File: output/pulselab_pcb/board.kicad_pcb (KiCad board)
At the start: 2 copper layers, 60 x 60 mm, 17 parts

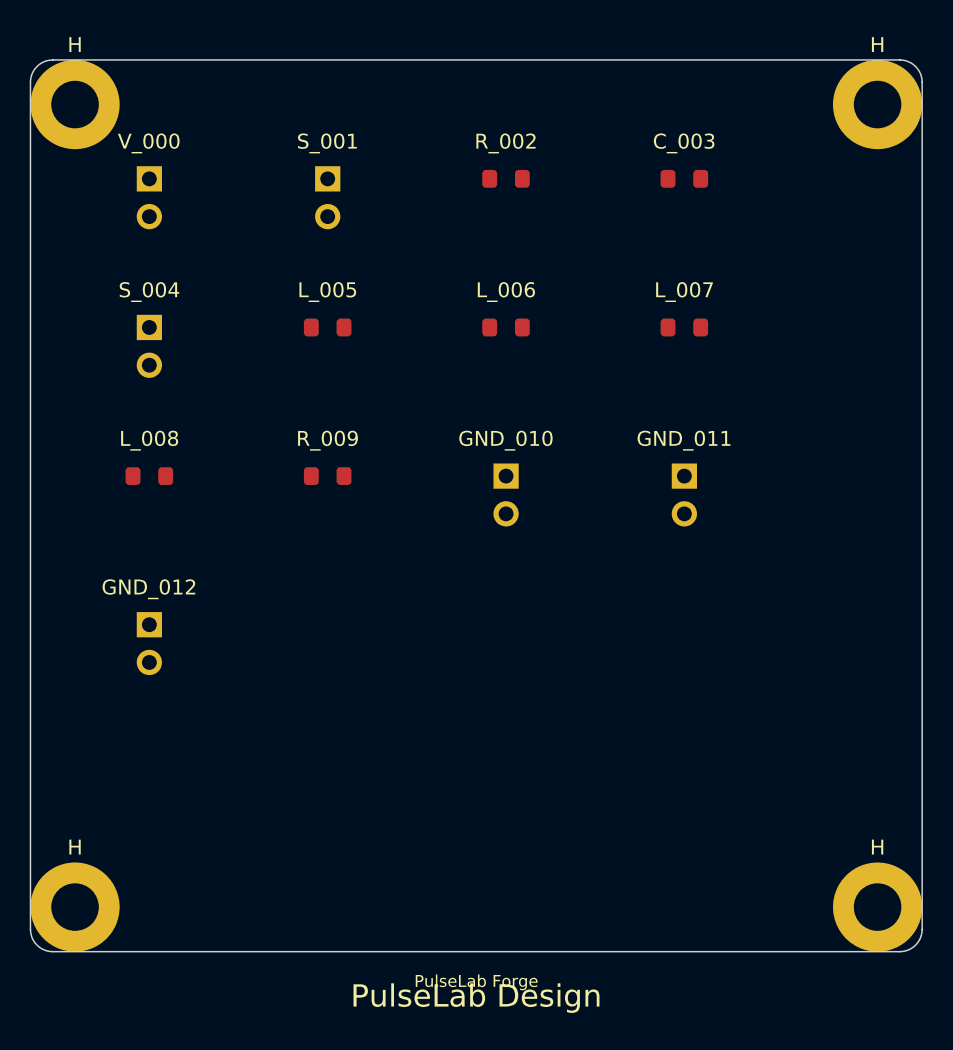
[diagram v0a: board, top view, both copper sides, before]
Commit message: chore: update dependencies and project artifacts
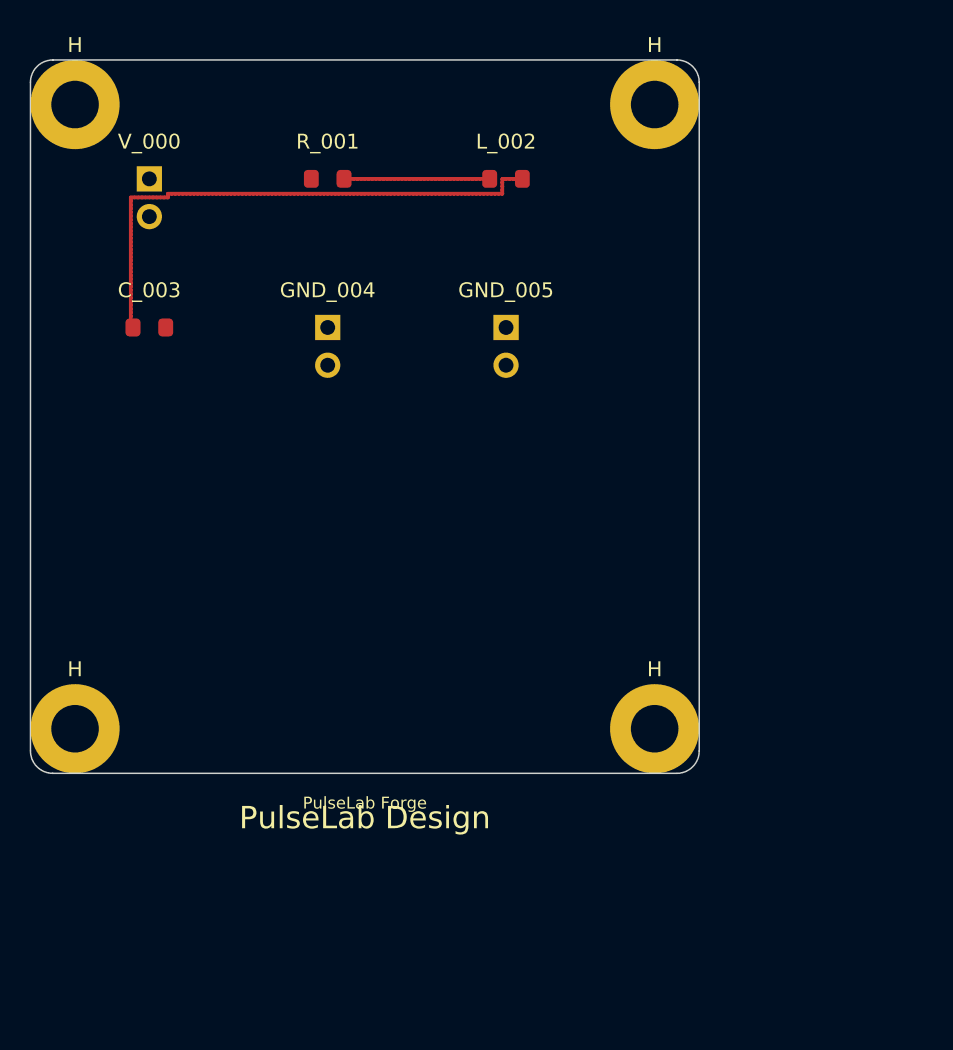
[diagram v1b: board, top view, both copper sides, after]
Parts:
- removed GND_010, GND_011, GND_012: GND, Connector_PinHeader_2.54mm:PinHeader_1x02_P2.54mm_Vertical
- removed the H at (57.0, 3.00)
- removed the H at (3.00, 57.0)
- removed the H at (57.0, 57.0)
- removed L_005, L_006, L_007, L_008: 2.5e-07, Inductor_SMD:L_0805_2012Metric
- removed R_002: 10000, Resistor_SMD:R_0805_2012Metric
- removed R_009: 50, Resistor_SMD:R_0805_2012Metric
- removed S_001, S_004: S, Connector_PinHeader_2.54mm:PinHeader_1x02_P2.54mm_Vertical
- added GND_004: GND, Connector_PinHeader_2.54mm:PinHeader_1x02_P2.54mm_Vertical, F.Cu at (20.0, 18.0)
- added GND_005: GND, Connector_PinHeader_2.54mm:PinHeader_1x02_P2.54mm_Vertical, F.Cu at (32.0, 18.0)
- added H: , MountingHole:MountingHole_3.2mm_M3, F.Cu at (42.0, 3.00)
- added H: , MountingHole:MountingHole_3.2mm_M3, F.Cu at (3.00, 45.0)
- added H: , MountingHole:MountingHole_3.2mm_M3, F.Cu at (42.0, 45.0)
- added L_002: 0.001, Inductor_SMD:L_0805_2012Metric, F.Cu at (32.0, 8.00)
- added R_001: 10, Resistor_SMD:R_0805_2012Metric, F.Cu at (20.0, 8.00)
- C_003: value 6e-07 -> 1e-05
- V_000: value 5000V -> 24V
- moved C_003 37.4 mm to (8.00, 18.0)
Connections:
- C_003 pad 1: BANCO -> M2
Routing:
- net M2: track 0.00 -> 36.4 mm
- net M1: track 0.00 -> 9.90 mm
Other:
- board size 60 x 60 mm -> 45 x 48 mm

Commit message: feat: implement PCB editor with component placement, multi-selection, and wire routing capabilities
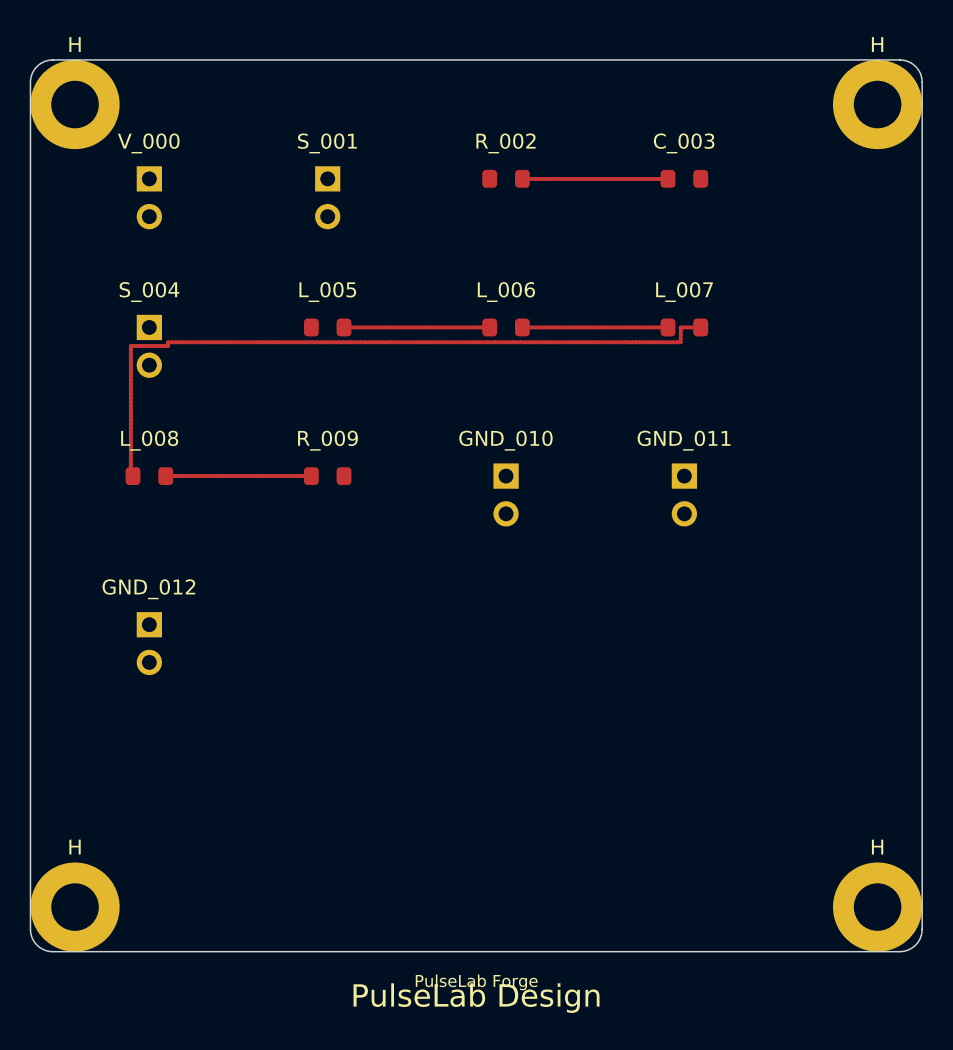
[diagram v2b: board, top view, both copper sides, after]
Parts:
- removed GND_004, GND_005: GND, Connector_PinHeader_2.54mm:PinHeader_1x02_P2.54mm_Vertical
- removed the H at (42.0, 3.00)
- removed the H at (3.00, 45.0)
- removed the H at (42.0, 45.0)
- removed L_002: 0.001, Inductor_SMD:L_0805_2012Metric
- removed R_001: 10, Resistor_SMD:R_0805_2012Metric
- added GND_010: GND, Connector_PinHeader_2.54mm:PinHeader_1x02_P2.54mm_Vertical, F.Cu at (32.0, 28.0)
- added GND_011: GND, Connector_PinHeader_2.54mm:PinHeader_1x02_P2.54mm_Vertical, F.Cu at (44.0, 28.0)
- added GND_012: GND, Connector_PinHeader_2.54mm:PinHeader_1x02_P2.54mm_Vertical, F.Cu at (8.00, 38.0)
- added H: , MountingHole:MountingHole_3.2mm_M3, F.Cu at (57.0, 3.00)
- added H: , MountingHole:MountingHole_3.2mm_M3, F.Cu at (3.00, 57.0)
- added H: , MountingHole:MountingHole_3.2mm_M3, F.Cu at (57.0, 57.0)
- added L_005: 2.5e-07, Inductor_SMD:L_0805_2012Metric, F.Cu at (20.0, 18.0)
- added L_006: 2.5e-07, Inductor_SMD:L_0805_2012Metric, F.Cu at (32.0, 18.0)
- added L_007: 2.5e-07, Inductor_SMD:L_0805_2012Metric, F.Cu at (44.0, 18.0)
- added L_008: 2.5e-07, Inductor_SMD:L_0805_2012Metric, F.Cu at (8.00, 28.0)
- added R_002: 10000, Resistor_SMD:R_0805_2012Metric, F.Cu at (32.0, 8.00)
- added R_009: 50, Resistor_SMD:R_0805_2012Metric, F.Cu at (20.0, 28.0)
- added S_001: S, Connector_PinHeader_2.54mm:PinHeader_1x02_P2.54mm_Vertical, F.Cu at (20.0, 8.00)
- added S_004: S, Connector_PinHeader_2.54mm:PinHeader_1x02_P2.54mm_Vertical, F.Cu at (8.00, 18.0)
- C_003: value 1e-05 -> 6e-07
- V_000: value 24V -> 5000V
- moved C_003 37.4 mm to (44.0, 8.00)
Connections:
- C_003 pad 1: M2 -> BANCO
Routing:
- net PFN3: track 0.00 -> 48.4 mm
- net M2: track 36.4 -> 0.00 mm
- net PFN2: track 0.00 -> 9.90 mm
- net PFN1: track 0.00 -> 9.90 mm
- net M1: track 9.90 -> 0.00 mm
- net BANCO: track 0.00 -> 9.90 mm
- net ANT_IN: track 0.00 -> 9.90 mm
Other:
- board size 45 x 48 mm -> 60 x 60 mm
